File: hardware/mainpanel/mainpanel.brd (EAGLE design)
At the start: 80 x 80 mm, 26 parts, among them J1 CDH, J2 OW, J3 DBG, J4 SUN-UART, J5 ADCS, J6 ENV, J7 SUN, U1 DS18B20, U2 DS18B20, U3 DS18B20

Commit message: Add trestrict for autorouter
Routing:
- net TEMP-OW: track 3.64 -> 31.9 mm
- net IMU-SCL: track 0.00 -> 23.1 mm
- net SPI-SCK: track 0.00 -> 22.0 mm
- net SPI-MOSI: track 0.00 -> 22.0 mm
- net SPI-MISO: track 0.00 -> 22.0 mm
- net LOG-UART: track 0.00 -> 18.8 mm
- net GPS-SCL: track 0.00 -> 6.20 mm
- net GPS-SDA: track 0.00 -> 4.99 mm
- net IMU-SDA: track 0.00 -> 4.47 mm
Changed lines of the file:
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@@
 <setting verticaltext="up"/>
 </settings>
-<grid distance="1" unitdist="mm" unit="mm" style="lines" multiple="1" display="yes" altdistance="5" altunitdist="mil" altunit="mil"/>
+<grid distance="0.1" unitdist="mm" unit="mm" style="lines" multiple="1" display="yes" altdistance="5" altunitdist="mil" altunit="mil"/>
 <layers>
 <layer number="1" name="Top" color="4" fill="1" visible="yes" active="yes"/>
@@
 <wire x1="5" y1="25" x2="0" y2="25" width="0.1524" layer="21"/>
 <wire x1="5" y1="26" x2="0" y2="26" width="0.1524" layer="21"/>
+<rectangle x1="10" y1="51" x2="26" y2="55" layer="41"/>
+<rectangle x1="10" y1="62" x2="26" y2="66" layer="41"/>
+<rectangle x1="10" y1="73" x2="26" y2="77" layer="41"/>
+<rectangle x1="27" y1="73" x2="36" y2="77" layer="41"/>
+<rectangle x1="38" y1="73" x2="54" y2="77" layer="41"/>
+<rectangle x1="41" y1="59" x2="51" y2="63" layer="41"/>
+<rectangle x1="58" y1="48" x2="73" y2="51" layer="41"/>
+<rectangle x1="58" y1="23" x2="74" y2="26" layer="41"/>
+<rectangle x1="32" y1="23" x2="47" y2="26" layer="41"/>
+<rectangle x1="7" y1="8" x2="15" y2="12" layer="41"/>
+<rectangle x1="9" y1="40" x2="19" y2="44" layer="41"/>
+<rectangle x1="9" y1="29" x2="19" y2="33" layer="41"/>
+<circle x="28.3" y="44.5" radius="0.721109375" width="0.4" layer="41"/>
+<circle x="30.9" y="44.5" radius="0.721109375" width="0.4" layer="41"/>
+<circle x="33.4" y="44.5" radius="0.721109375" width="0.4" layer="41"/>
+<circle x="35.9" y="44.5" radius="0.721109375" width="0.4" layer="41"/>
+<circle x="43.6" y="44.5" radius="0.721109375" width="0.4" layer="41"/>
+<circle x="46.1" y="44.5" radius="0.721109375" width="0.4" layer="41"/>
+<circle x="48.7" y="44.5" radius="0.721109375" width="0.4" layer="41"/>
+<circle x="51.2" y="44.5" radius="0.721109375" width="0.4" layer="41"/>
+<circle x="53.7" y="44.5" radius="0.721109375" width="0.4" layer="41"/>
+<circle x="48.7" y="29.2" radius="0.721109375" width="0.4" layer="41"/>
+<circle x="46.2" y="29.2" radius="0.721109375" width="0.4" layer="41"/>
+<circle x="43.6" y="29.2" radius="0.721109375" width="0.4" layer="41"/>
+<circle x="41.1" y="29.2" radius="0.721109375" width="0.4" layer="41"/>
+<circle x="38.5" y="29.2" radius="0.721109375" width="0.4" layer="41"/>
+<circle x="36" y="29.2" radius="0.721109375" width="0.4" layer="41"/>
+<circle x="36" y="50" radius="0.721109375" width="0.4" layer="41"/>
 </plain>
 <attributes>
@@
 <param name="RoutingGrid" value="0.125mm"/>
 <param name="AutoGrid" value="1"/>
-<param name="Efforts" value="1"/>
+<param name="Efforts" value="2"/>
 <param name="TopRouterVariant" value="1"/>
 <param name="tpViaShape" value="round"/>
@@
 <contactref element="B1" pad="D12"/>
 <contactref element="R4" pad="2"/>
+<wire x1="38.4" y1="24.66" x2="38.4" y2="22.45" width="0.2" layer="16"/>
+<wire x1="38.4" y1="22.45" x2="40" y2="20.85" width="0.2" layer="16"/>
 <wire x1="38.4" y1="24.66" x2="28.35" y2="44.48" width="0" layer="19" extent="1-1"/>
-<wire x1="40" y1="20.85" x2="38.4" y2="24.66" width="0" layer="19" extent="16-16"/>
 </signal>
 <signal name="IMU-SCL">
@@
 <contactref element="B1" pad="A6"/>
 <contactref element="R3" pad="2"/>
-<wire x1="35.86" y1="24.66" x2="51.21" y2="29.24" width="0" layer="19" extent="1-1"/>
-<wire x1="34" y1="20.85" x2="35.86" y2="24.66" width="0" layer="19" extent="16-16"/>
+<wire x1="35.86" y1="24.66" x2="35.86" y2="22.71" width="0.2" layer="16"/>
+<wire x1="35.86" y1="22.71" x2="34" y2="20.85" width="0.2" layer="16"/>
+<wire x1="35.86" y1="24.66" x2="35.86" y2="25.86" width="0.2" layer="16"/>
+<wire x1="35.86" y1="25.86" x2="37" y2="27" width="0.2" layer="16"/>
+<wire x1="37" y1="27" x2="50" y2="27" width="0.2" layer="16"/>
+<wire x1="50" y1="27" x2="51.21" y2="28.21" width="0.2" layer="16"/>
+<wire x1="51.21" y1="28.21" x2="51.21" y2="29.24" width="0.2" layer="16"/>
 </signal>
 <signal name="GRN">
@@
 <contactref element="B1" pad="D4"/>
 <contactref element="R6" pad="2"/>
-<wire x1="59.27" y1="49.27" x2="59" y2="54.15" width="0" layer="19" extent="16-16"/>
+<wire x1="59.27" y1="49.27" x2="59.27" y2="53.88" width="0.2" layer="16"/>
+<wire x1="59.27" y1="53.88" x2="59" y2="54.15" width="0.2" layer="16"/>
 <wire x1="48.67" y1="44.48" x2="59.27" y2="49.27" width="0" layer="19" extent="1-1"/>
 </signal>
@@
 <contactref element="B1" pad="D5"/>
 <contactref element="R5" pad="2"/>
-<wire x1="61.81" y1="49.27" x2="65" y2="54.15" width="0" layer="19" extent="16-16"/>
+<wire x1="61.81" y1="49.27" x2="61.81" y2="50.96" width="0.2" layer="16"/>
+<wire x1="61.81" y1="50.96" x2="65" y2="54.15" width="0.2" layer="16"/>
 <wire x1="46.13" y1="44.48" x2="61.81" y2="49.27" width="0" layer="19" extent="1-1"/>
 </signal>
@@
 <contactref element="B4" pad="RXI"/>
 <contactref element="B1" pad="A7"/>
-<wire x1="53.75" y1="29.24" x2="69.81" y2="24.128" width="0" layer="19" extent="1-1"/>
+<wire x1="53.75" y1="29.24" x2="55.99" y2="27" width="0.2" layer="16"/>
+<wire x1="68" y1="27" x2="69.81" y2="25.19" width="0.2" layer="16"/>
+<wire x1="69.81" y1="25.19" x2="69.81" y2="24.128" width="0.2" layer="16"/>
+<wire x1="55.99" y1="27" x2="68" y2="27" width="0.2" layer="16"/>
 </signal>
 <signal name="CDH-TX">
@@
 <contactref element="J5" pad="5"/>
 <contactref element="J7" pad="5"/>
+<wire x1="14.19" y1="75" x2="14.19" y2="64" width="0.2" layer="16"/>
+<wire x1="14.19" y1="64" x2="14.19" y2="53" width="0.2" layer="16"/>
 <wire x1="14.19" y1="53" x2="53.75" y2="44.48" width="0" layer="19" extent="1-1"/>
-<wire x1="14.19" y1="64" x2="14.19" y2="53" width="0" layer="19" extent="1-1"/>
-<wire x1="14.19" y1="75" x2="14.19" y2="64" width="0" layer="19" extent="1-1"/>
 </signal>
 <signal name="SPI-CS-ADCS">
@@
 <wire x1="36" y1="40.85" x2="36" y2="44.45" width="0.2" layer="16"/>
 <wire x1="36" y1="44.45" x2="35.97" y2="44.48" width="0.2" layer="16"/>
+<wire x1="15.27" y1="31" x2="15.27" y2="14.27" width="0.2" layer="16"/>
+<wire x1="15.27" y1="14.27" x2="11" y2="10" width="0.2" layer="16"/>
+<wire x1="35.97" y1="44.48" x2="35.97" y2="49.97" width="0.2" layer="16"/>
+<wire x1="35.97" y1="49.97" x2="36" y2="50" width="0.2" layer="16"/>
 <wire x1="36" y1="50" x2="32" y2="75" width="0" layer="19" extent="1-1"/>
-<wire x1="35.97" y1="44.48" x2="36" y2="50" width="0" layer="19" extent="1-1"/>
 <wire x1="15.27" y1="31" x2="36" y2="40.85" width="0" layer="19" extent="16-16"/>
-<wire x1="11" y1="10" x2="15.27" y2="31" width="0" layer="19" extent="1-1"/>
 </signal>
 <signal name="SPI-SCK">
@@
 <contactref element="J5" pad="2"/>
 <contactref element="J7" pad="2"/>
-<wire x1="21.81" y1="64" x2="21.81" y2="75" width="0" layer="19" extent="1-1"/>
-<wire x1="21.81" y1="53" x2="21.81" y2="64" width="0" layer="19" extent="1-1"/>
+<wire x1="21.81" y1="75" x2="21.81" y2="64" width="0.2" layer="16"/>
+<wire x1="21.81" y1="64" x2="21.81" y2="53" width="0.2" layer="16"/>
 <wire x1="38.51" y1="29.24" x2="21.81" y2="53" width="0" layer="19" extent="1-1"/>
 </signal>
@@
 <contactref element="J5" pad="4"/>
 <contactref element="J7" pad="4"/>
-<wire x1="16.73" y1="64" x2="16.73" y2="75" width="0" layer="19" extent="1-1"/>
-<wire x1="16.73" y1="53" x2="16.73" y2="64" width="0" layer="19" extent="1-1"/>
-<wire x1="48.67" y1="29.24" x2="16.73" y2="53" width="0" layer="19" extent="1-1"/>
+<wire x1="16.73" y1="75" x2="16.73" y2="64" width="0.2" layer="16"/>
+<wire x1="16.73" y1="64" x2="16.73" y2="53" width="0.2" layer="16"/>
+<wire x1="16.73" y1="53" x2="48.67" y2="29.24" width="0" layer="19" extent="1-1"/>
 </signal>
 <signal name="SPI-CS-ENV">

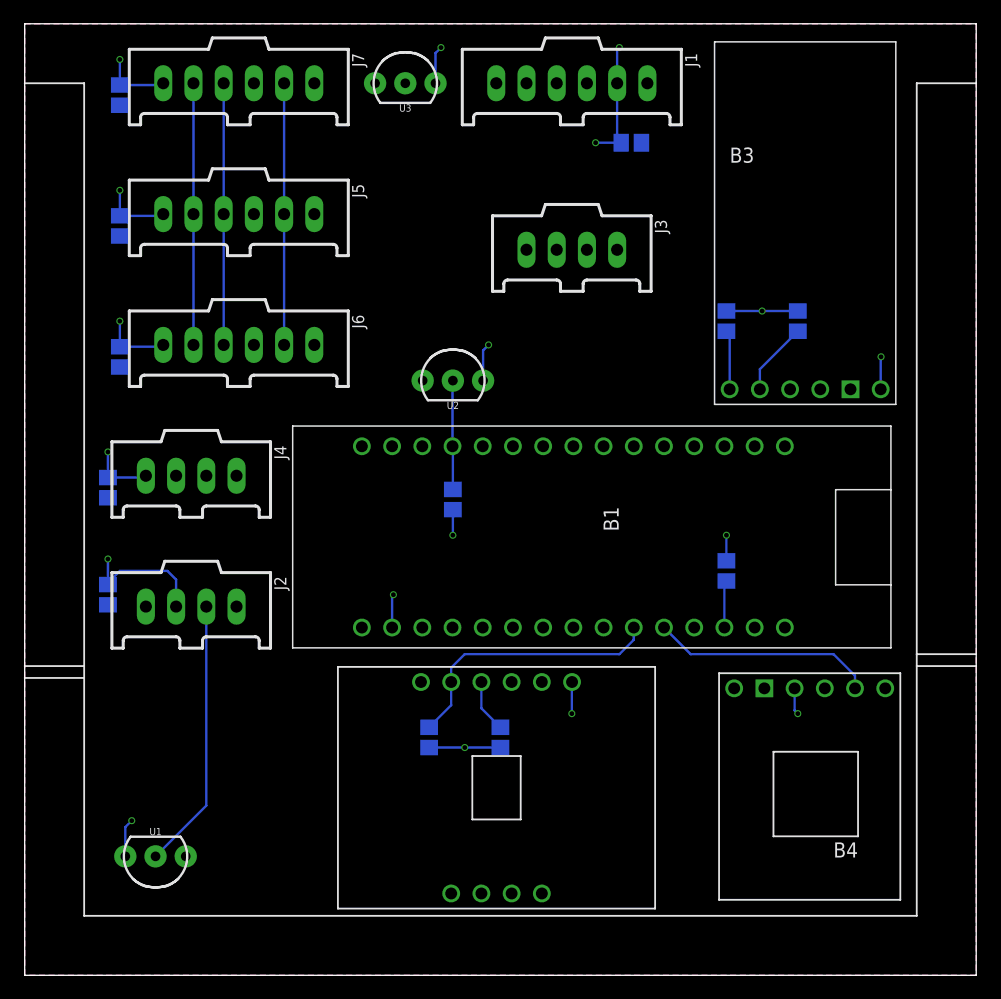
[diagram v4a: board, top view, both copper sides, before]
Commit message: Connect board components
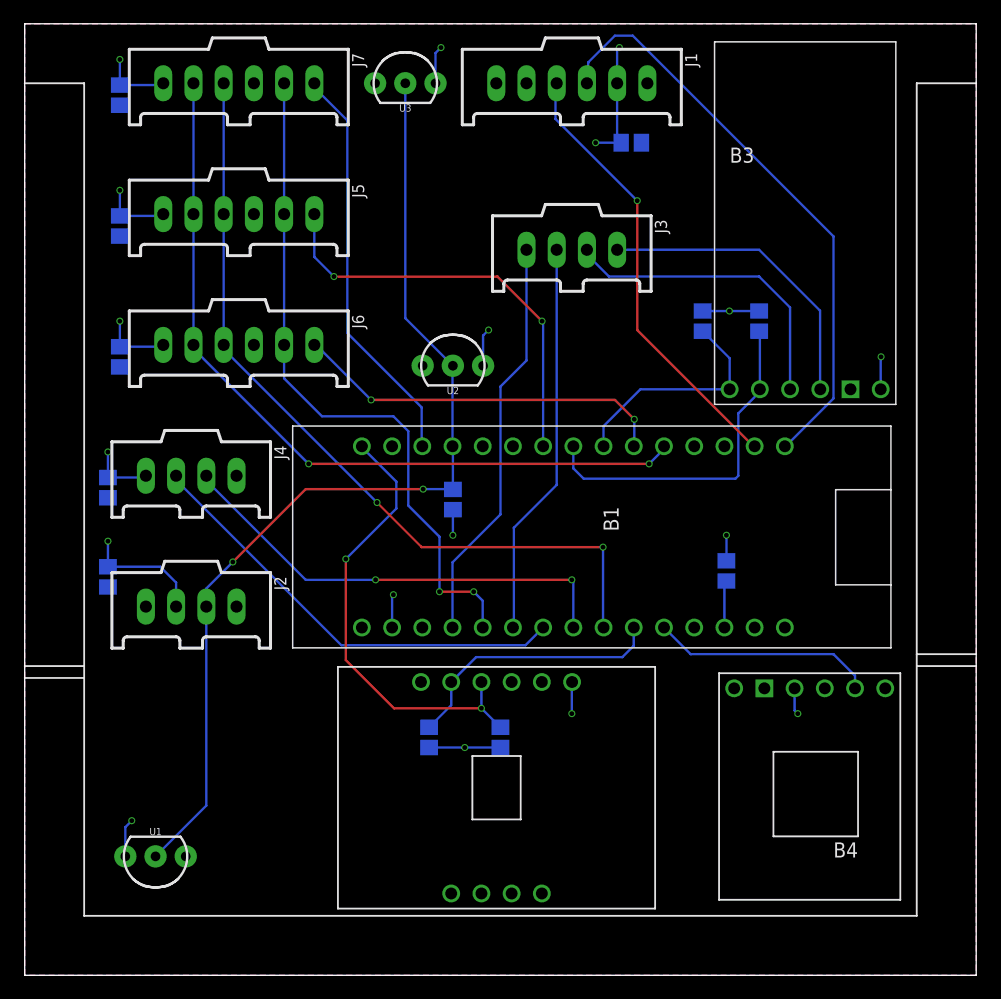
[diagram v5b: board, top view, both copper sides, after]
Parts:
- moved R5 3.25 mm to (61.8, 55.0)
- moved R6 2.00 mm to (57.0, 55.0)
- moved C2 1.50 mm to (7.00, 33.5)
- moved U2 1.25 mm to (36.0, 51.2)
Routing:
- net TEMP-OW: track 31.9 -> 84.5 mm, vias 0 -> 2
- net CDH-TX: track 0.00 -> 49.8 mm
- net SPI-MISO: track 22.0 -> 68.0 mm, vias 0 -> 2
- net SPI-MOSI: track 22.0 -> 66.7 mm, vias 0 -> 2
- net SUN-RX: track 0.00 -> 38.7 mm, vias 0 -> 2
- net CDH-RX: track 0.00 -> 37.6 mm, vias 0 -> 1
- net SUN-TX: track 0.00 -> 37.6 mm
- net SPI-SCK: track 22.0 -> 57.9 mm, vias 0 -> 2
- net SPI-CS-ADCS: track 0.00 -> 35.5 mm, vias 0 -> 2
- net DBG-TX: track 0.00 -> 34.3 mm
- net SPI-CS-SUN: track 0.00 -> 34.3 mm
- net IMU-SDA: track 4.47 -> 38.5 mm, vias 0 -> 2
- net DBG-RX: track 0.00 -> 33.3 mm
- net SPI-CS-ENV: track 0.00 -> 31.8 mm, vias 0 -> 2
- net GPS-TX: track 0.00 -> 26.3 mm
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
